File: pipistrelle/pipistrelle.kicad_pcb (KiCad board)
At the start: 2 copper layers, 38 x 100 mm, 67 parts, among them J1 C2M, J2 C2F, J3 Eurorack Power, J4 CV1, J5 V/OCT, J6 OUT, J7 CV2, J8 C1M, J9 C1F, U1 SeeeduinoXIAO, U2 MCP6002-xSN, U3 MCP6002-xSN, U4 TL072, U5 LM1117-5.0, U6 LM4040DBZ-10

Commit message: Give it a name: Pipistrelle
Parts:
- D1, D2: value SM4001 -> SM4007PL; footprint Diode_THT:D_DO-41_SOD81_P10.16mm_Horizontal -> Personal:SOD-123FL
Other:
- board text added: "Pipistrelle Rev. 1 Paul Battley 2022 CC-BY-SA-4.0"
- board text removed: "Nostrum Rev. 1 Paul Battley 2022 CC-BY-SA-4.0"

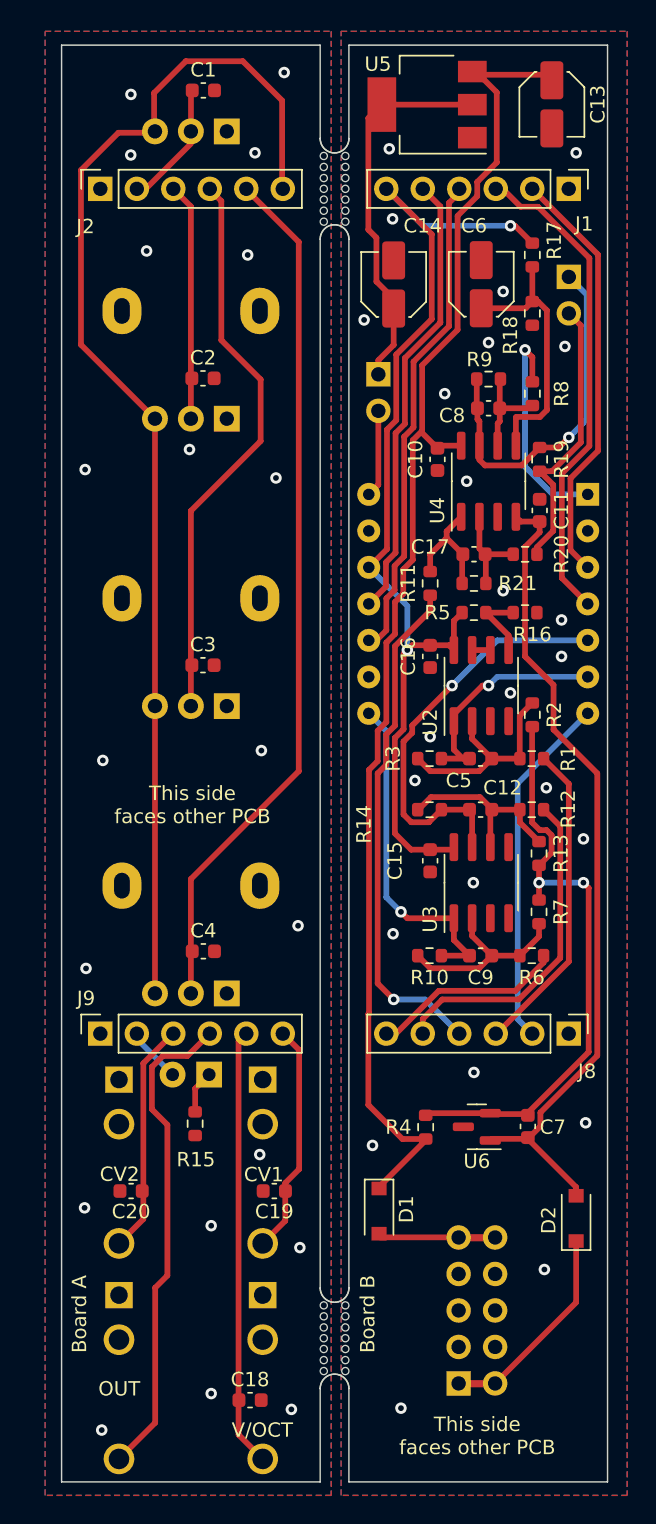
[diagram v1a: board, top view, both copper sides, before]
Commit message: Added power caps
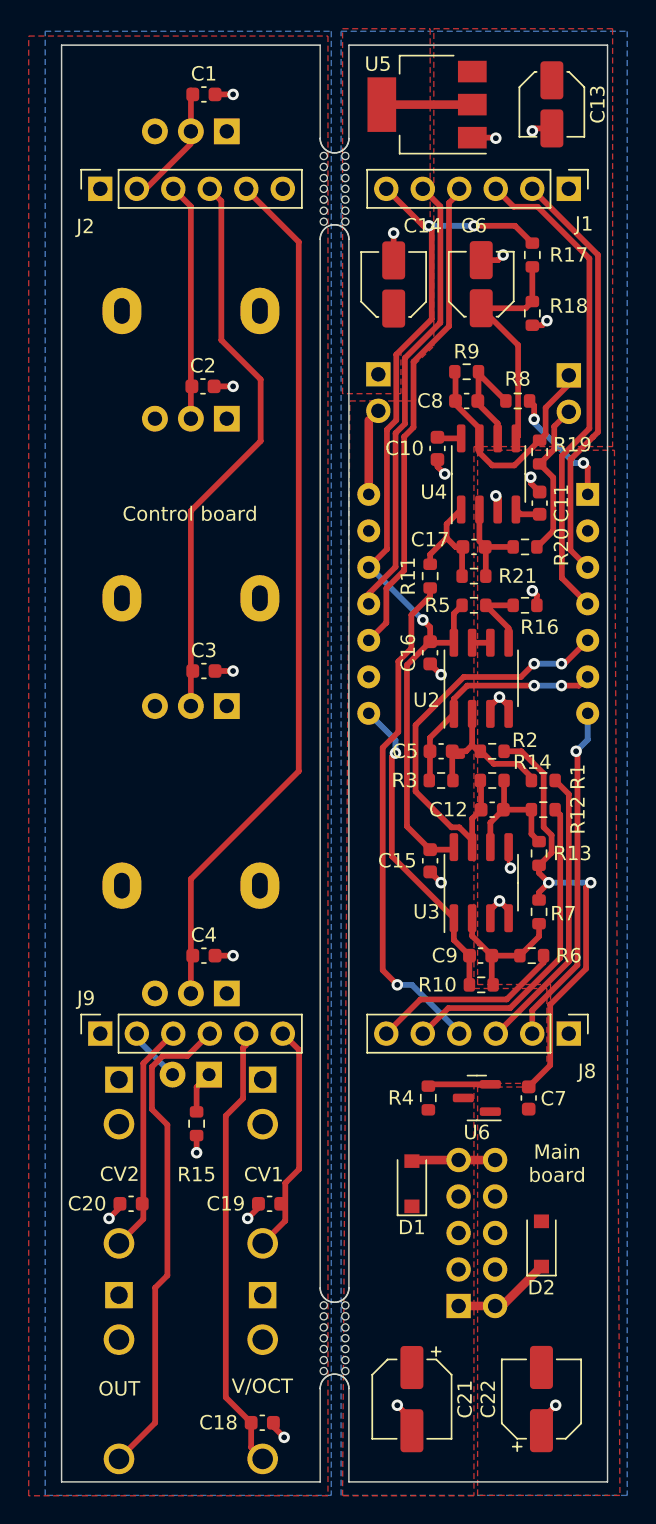
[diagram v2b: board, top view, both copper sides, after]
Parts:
- added C21: 22u, Capacitor_SMD:CP_Elec_5x5.9, F.Cu at (174.4, 144.2)
- added C22: 22u, Capacitor_SMD:CP_Elec_5x5.9, F.Cu at (183.4, 144.2)
- moved JP2 6.85 mm to (185.3, 73.0)
- moved J3 5.39 mm to (177.6, 137.8)
- moved R14 4.81 mm to (180.0, 101.2), turned to 180 degrees
- moved R10 4.13 mm to (179.2, 115.4), turned to 180 degrees
- moved R2 3.78 mm to (180.0, 99.1), turned to 180 degrees
- moved D2 3.00 mm to (183.4, 133.4)
- moved D1 2.98 mm to (174.4, 129.2), turned to 90 degrees
- moved C5 2.80 mm to (176.4, 99.1)
- moved R4 2.04 mm to (175.5, 123.3)
- moved U6 2.01 mm to (178.9, 123.3)
- moved C7 1.98 mm to (182.5, 123.3)
- moved C18 1.79 mm to (164.0, 145.9)
- moved R1 1.72 mm to (183.5, 101.2)
- moved R3 1.72 mm to (176.4, 101.2), turned to 180 degrees
- moved C8 1.61 mm to (178.2, 74.8)
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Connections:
- J8 pad 1: GND -> unconnected-(J8-Pad1)
- J9 pad 1: GND1 -> unconnected-(J9-Pad1)
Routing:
- net +12V: track 94.7 -> 1.93 mm
- net /CONN_3V3: track 85.6 -> 0.12 mm
- net -12V: track 57.3 -> 1.79 mm
- net GND: track 0.00 -> 27.5 mm, vias 24 -> 16
- net +5V: track 26.6 -> 6.30 mm
- net GND1: track 0.00 -> 10.3 mm, vias 20 -> 8
- net Net-(JP2-Pad2): track 19.7 -> 11.1 mm
- net Net-(C8-Pad1): track 25.1 -> 17.0 mm, vias 1 -> 0
- net Net-(J3-Pad1): track 14.8 -> 6.90 mm
- net /AUDIO_OUT: track 15.7 -> 8.55 mm, vias 1 -> 2
- net +3V3: track 72.2 -> 66.5 mm, vias 2 -> 3
- net /VREF_-10: track 41.5 -> 37.1 mm
- net Net-(C9-Pad1): track 13.8 -> 9.97 mm
- net Net-(C12-Pad1): track 13.2 -> 9.43 mm
- net Net-(C5-Pad1): track 15.2 -> 11.9 mm
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- added copper zone on F.Cu, net +12V
- added copper zone on F.Cu, net +5V
- added copper zone on F.Cu, net -12V
- added copper zone on F.Cu, net /CONN_3V3
- removed copper zone on F.Cu, net GND
- removed copper zone on F.Cu, net GND1
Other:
- board text added: "Control board"
- board text added: "Main board"
- board text added: "Output range ±5V/±8V"
- board text added: "Remove → before plugging USB!"
- board text added: "µC 5V supply"
- board text removed: "Board A"
- board text removed: "Board B"
- board text removed: "This side faces other PCB"
- board text removed: "µC 5V supply → Remove before plugging USB!"
- board text removed: "← Output range with: ±8V without: ±5V"

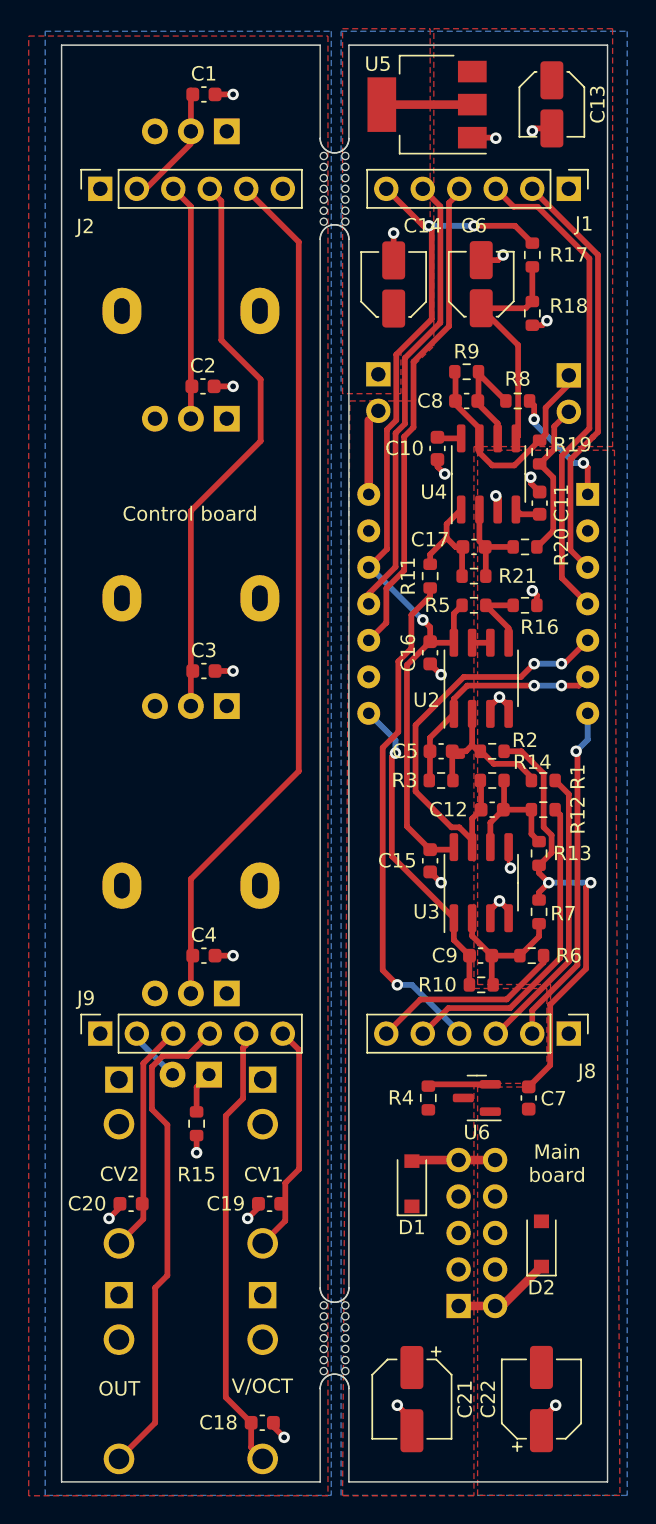
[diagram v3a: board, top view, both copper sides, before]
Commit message: Tidied up edge cuts
Some weird .999999 measurements had crept in.
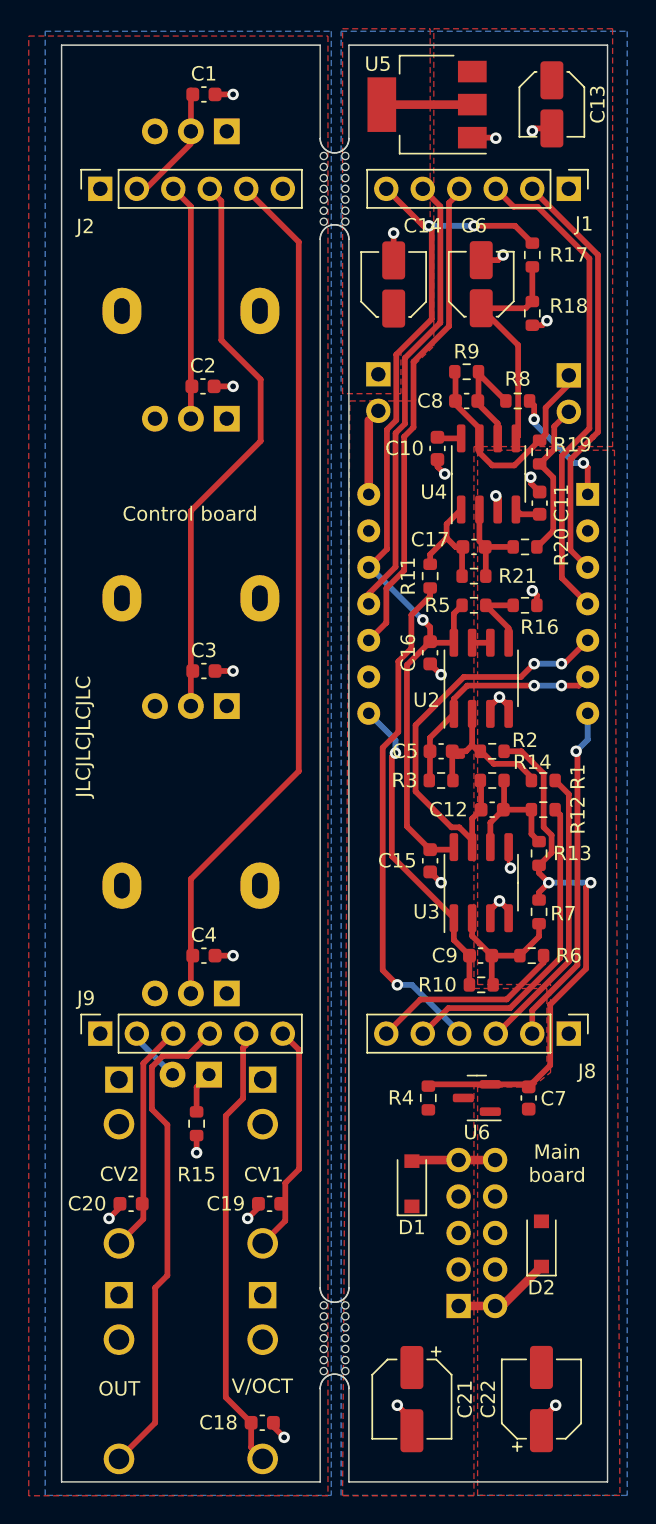
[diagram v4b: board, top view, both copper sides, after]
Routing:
- net /VREF_-10: track 37.1 -> 39.4 mm
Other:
- board text added: "JLCJLCJLCJLC"
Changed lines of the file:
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@@
     (pad_to_mask_clearance 0)
     (solder_mask_min_width 0.12)
-    (grid_origin 171.082 113.373)
+    (grid_origin 179.21 108.293)
     (pcbplotparams
       (layerselection 0x00010fc_ffffffff)
@@
   (gr_line (start 150 50) (end 168 50) (layer "Edge.Cuts") (width 0.1))
   (gr_line (start 168 150) (end 150 150) (layer "Edge.Cuts") (width 0.1))
-  (gr_arc (start 167.9992 63.5) (mid 168.9992 62.5) (end 169.9992 63.5) (layer "Edge.Cuts") (width 0.1))
-  (gr_line (start 168 136.5) (end 167.9992 63.5) (layer "Edge.Cuts") (width 0.1))
-  (gr_line (start 169.9992 56.5) (end 170 50) (layer "Edge.Cuts") (width 0.1))
+  (gr_arc (start 168 63.5) (mid 169 62.5) (end 170 63.5) (layer "Edge.Cuts") (width 0.1))
+  (gr_line (start 168 136.5) (end 168 63.5) (layer "Edge.Cuts") (width 0.1))
+  (gr_line (start 170 56.5) (end 170 50) (layer "Edge.Cuts") (width 0.1))
   (gr_line (start 188 150) (end 188 50) (layer "Edge.Cuts") (width 0.1))
-  (gr_arc (start 167.9992 143.5) (mid 168.9992 142.5) (end 169.9992 143.5) (layer "Edge.Cuts") (width 0.1))
+  (gr_arc (start 168 143.5) (mid 169 142.5) (end 170 143.5) (layer "Edge.Cuts") (width 0.1))
   (gr_line (start 188 150) (end 170 150) (layer "Edge.Cuts") (width 0.1))
-  (gr_arc (start 169.9992 56.5) (mid 168.9992 57.5) (end 167.9992 56.5) (layer "Edge.Cuts") (width 0.1))
-  (gr_line (start 167.9992 143.5) (end 168 150) (layer "Edge.Cuts") (width 0.1))
+  (gr_arc (start 170 56.5) (mid 169 57.5) (end 168 56.5) (layer "Edge.Cuts") (width 0.1))
+  (gr_line (start 168 143.5) (end 168 150) (layer "Edge.Cuts") (width 0.1))
   (gr_line (start 170 50) (end 188 50) (layer "Edge.Cuts") (width 0.1))
   (gr_line (start 150 150) (end 150 50) (layer "Edge.Cuts") (width 0.1))
-  (gr_line (start 170 150) (end 169.9992 143.5) (layer "Edge.Cuts") (width 0.1))
-  (gr_line (start 168 50) (end 167.9992 56.5) (layer "Edge.Cuts") (width 0.1))
-  (gr_line (start 169.9992 63.5) (end 170 136.5) (layer "Edge.Cuts") (width 0.1))
+  (gr_line (start 170 150) (end 170 143.5) (layer "Edge.Cuts") (width 0.1))
+  (gr_line (start 168 50) (end 168 56.5) (layer "Edge.Cuts") (width 0.1))
+  (gr_line (start 170 63.5) (end 170 136.5) (layer "Edge.Cuts") (width 0.1))
   (gr_arc (start 170 136.5) (mid 169 137.5) (end 168 136.5) (layer "Edge.Cuts") (width 0.1))
   (gr_line (start 179 40) (end 179 160) (layer "User.1") (width 0.15))
@@
   (gr_line (start 159 40) (end 159 160) (layer "User.1") (width 0.15))
   (gr_line (start 149.9964 48.5) (end 167.9964 48.5) (layer "User.1") (width 0.15))
-  (gr_text "← Red stripe down" (at 186.0934 138.0872 270) (layer "B.SilkS")
+  (gr_text "← Red stripe down" (at 186.0934 133.185 270) (layer "B.SilkS")
     (effects (font (size 1 1) (thickness 0.1524)) (justify mirror))
   )
@@
     (effects (font (size 1 1) (thickness 0.1524)) (justify mirror))
   )
+  (gr_text "JLCJLCJLCJLC" (at 151.524 98.133 90) (layer "F.SilkS")
+    (effects (font (size 1 1) (thickness 0.15)))
+  )
   (gr_text "OUT" (at 154.0132 143.5228) (layer "F.SilkS")
     (effects (font (size 1 1) (thickness 0.1524)))
@@
   (segment (start 184.10696 106.21148) (end 184.10696 104.987671) (width 0.4) (layer "F.Cu") (net 10))
   (segment (start 183.23244 109.5) (end 183.23244 108.96754) (width 0.4) (layer "F.Cu") (net 10))
+  (segment (start 179.8404 122.329) (end 182.337 122.329) (width 0.4) (layer "F.Cu") (net 10))
   (segment (start 183.23244 107.086) (end 183.23244 107.61846) (width 0.4) (layer "F.Cu") (net 10))
   (segment (start 183.55348 100.69848) (end 182.004 99.149) (width 0.4) (layer "F.Cu") (net 10))
@@
   (segment (start 183.23244 107.61846) (end 183.90698 108.293) (width 0.4) (layer "F.Cu") (net 10))
   (segment (start 186.83 108.293) (end 186.50504 108.61796) (width 0.4) (layer "F.Cu") (net 10))
-  (segment (start 179.8404 122.329) (end 180.2961 122.329) (width 0.4) (layer "F.Cu") (net 10))
   (segment (start 179.8404 122.329) (end 175.652 122.329) (width 0.4) (layer "F.Cu") (net 10))
   (segment (start 186.50504 108.61796) (end 186.50504 114.283798) (width 0.4) (layer "F.Cu") (net 10))
+  (segment (start 182.337 122.329) (end 182.512 122.504) (width 0.4) (layer "F.Cu") (net 10))
   (via (at 183.90698 108.293) (size 0.8) (drill 0.4) (layers "F.Cu" "B.Cu") (net 10))
   (via (at 186.83 108.293) (size 0.8) (drill 0.4) (layers "F.Cu" "B.Cu") (net 10))
@@
         (xy 178.956 150.940505)
         (xy 178.956 122.517)
-        (xy 182.639 122.517)
-        (xy 184.036 121.12)
+        (xy 182.766 122.517)
+        (xy 184.036 121.501)
         (xy 184.036 115.380505)
         (xy 178.956 115.380505)
@@
         (xy 183.782 115.659)
         (xy 183.782 121.12)
-        (xy 182.639 122.263)
+        (xy 182.512 122.263)
         (xy 178.702 122.263)
         (xy 178.702 130.645)
@@
     (connect_pads (clearance 0))
     (min_thickness 0.254)
-    (keepout (tracks not_allowed) (vias not_allowed) (pads not_allowed ) (copperpour not_allowed) (footprints not_allowed))
+    (keepout (tracks not_allowed) (vias not_allowed) (pads not_allowed ) (copperpour not_allowed) (footprints allowed))
     (fill (thermal_gap 0.508) (thermal_bridge_width 0.508))
     (polygon
@@
     (connect_pads (clearance 0))
     (min_thickness 0.254)
-    (keepout (tracks not_allowed) (vias not_allowed) (pads not_allowed ) (copperpour not_allowed) (footprints not_allowed))
+    (keepout (tracks not_allowed) (vias not_allowed) (pads not_allowed ) (copperpour not_allowed) (footprints allowed))
     (fill (thermal_gap 0.508) (thermal_bridge_width 0.508))
     (polygon
@@
     (connect_pads (clearance 0))
     (min_thickness 0.254)
-    (keepout (tracks not_allowed) (vias not_allowed) (pads not_allowed ) (copperpour not_allowed) (footprints not_allowed))
+    (keepout (tracks not_allowed) (vias not_allowed) (pads not_allowed ) (copperpour not_allowed) (footprints allowed))
     (fill (thermal_gap 0.508) (thermal_bridge_width 0.508))
     (polygon
@@
     (connect_pads (clearance 0))
     (min_thickness 0.254)
-    (keepout (tracks not_allowed) (vias not_allowed) (pads not_allowed ) (copperpour not_allowed) (footprints not_allowed))
+    (keepout (tracks not_allowed) (vias not_allowed) (pads not_allowed ) (copperpour not_allowed) (footprints allowed))
     (fill (thermal_gap 0.508) (thermal_bridge_width 0.508))
     (polygon
@@
     )
   )
+  (group "" (id 880844b1-5d83-436f-a471-030bc8715247)
+    (members
+      03de20c2-598b-489f-b509-163af49bcfb1
+      05cf9842-d0f1-4e86-9b87-1c870e953c32
+      18c8d1ea-ddea-4b74-9088-d367e8415921
+      2d1877f6-4b38-4c2f-b39d-f6bb4fd85b40
+      3525ce0c-cb33-40da-8c21-521ca8a6b7c8
+      3806e6ee-7673-4273-82d8-ec12dbdfacad
+      3c7e2ce7-dd92-4ca6-9440-c3fbac8c5d94
+      4b56b9ce-8ba8-476b-a405-ea60a86dfa24
+      563a8f3e-4950-4968-a633-0e884db0035b
+      844b981d-f8ec-4341-b74e-917fc0359d18
+      9ec0eb72-e3b0-41c7-81d7-40eaa7781c74
+      ab51780d-7829-4ba7-8e28-ff4c27d38ede
+      ad8ef11d-290c-480a-8eed-6ea7bf677943
+      b6c34a0b-5143-4190-a855-c15770abe3dc
+      bea8315b-2ce6-441a-ac7f-0b67cf9c79a3
+      f41a3b20-0292-48f5-835a-156a1e5cdd6f
+    )
+  )
